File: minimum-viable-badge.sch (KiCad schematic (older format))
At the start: 33 parts, among them J101 EDGE_CONNECTOR, P101 USB, P102 BATTERY, P103 POT_LONG, P104 BUTTON_A, P105 BUTTON_B, P106 POT_SHORT, P107 MECH, P108 MECH, P109 MECH, Q101 S8050, Q102 S8050, SW101 PRGM, SW102 RESET, U101 ESP32-WROOM, U102 CP2102

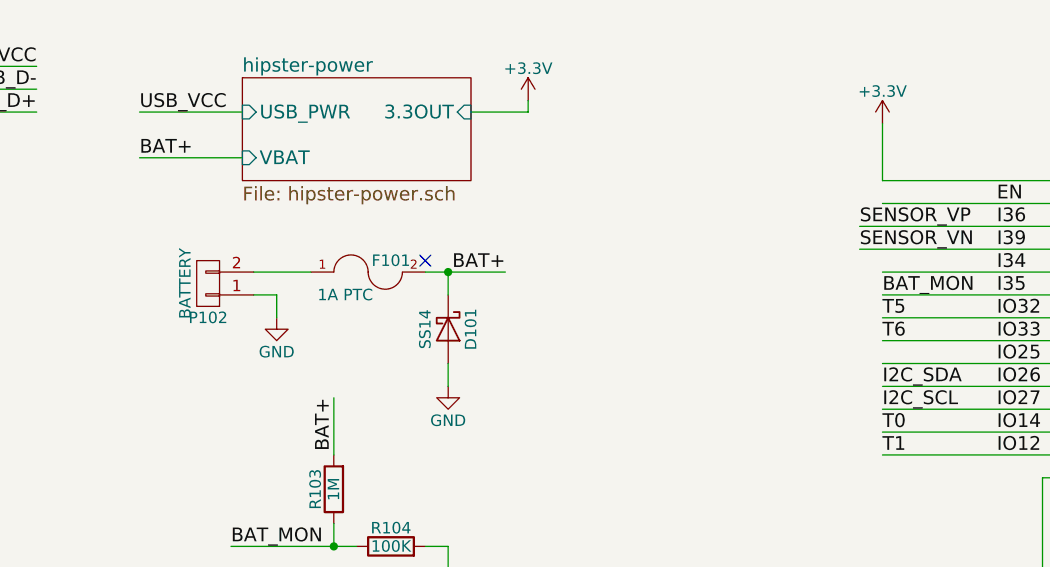
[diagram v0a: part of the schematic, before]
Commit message: Swap battery connector to JST PH 2.0
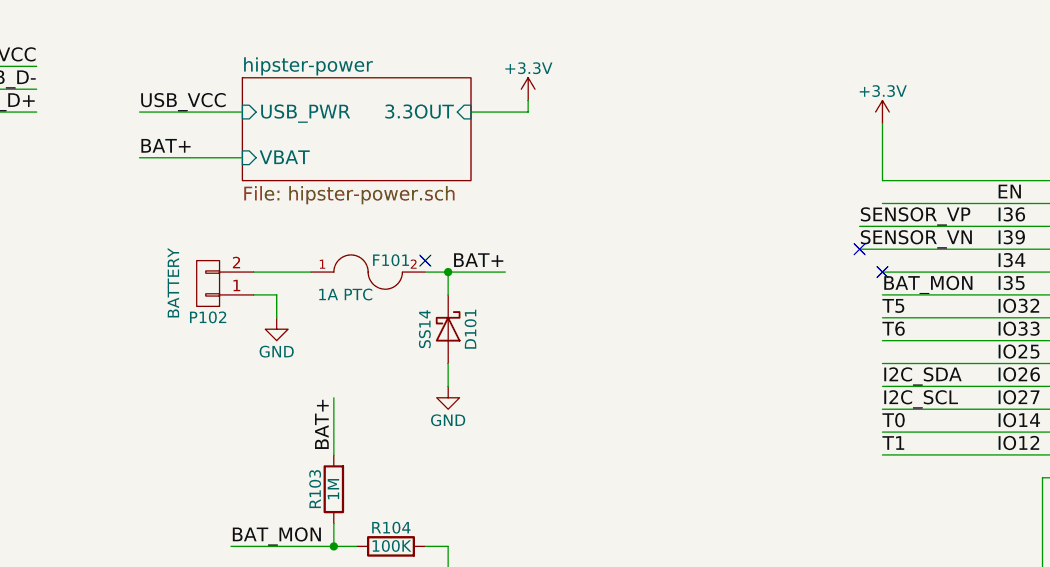
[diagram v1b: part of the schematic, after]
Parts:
- P102: footprint Pin_Headers:Pin_Header_Angled_1x02_Pitch2.54mm -> Connectors_JST:JST_PH_S2B-PH-K_02x2.00mm_Angled
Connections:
- no-connect marks 19 -> 21
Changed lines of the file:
@@
 P 2650 2100
 F 0 "P102" H 2650 2250 50  0000 C CNN
-F 1 "BATTERY" V 2750 2100 50  0000 C CNN
-F 2 "Pin_Headers:Pin_Header_Angled_1x02_Pitch2.54mm" H 2650 2100 50  0001 C CNN
+F 1 "BATTERY" V 2800 2100 50  0000 C CNN
+F 2 "Connectors_JST:JST_PH_S2B-PH-K_02x2.00mm_Angled" H 2650 2100 50  0001 C CNN
 F 3 "" H 2650 2100 50  0000 C CNN
 	1    2650 2100
@@
 Text Label 8550 1900 2    60   ~ 0
 IO21
+NoConn ~ 5500 1950
+NoConn ~ 5600 2050
 $EndSCHEMATC

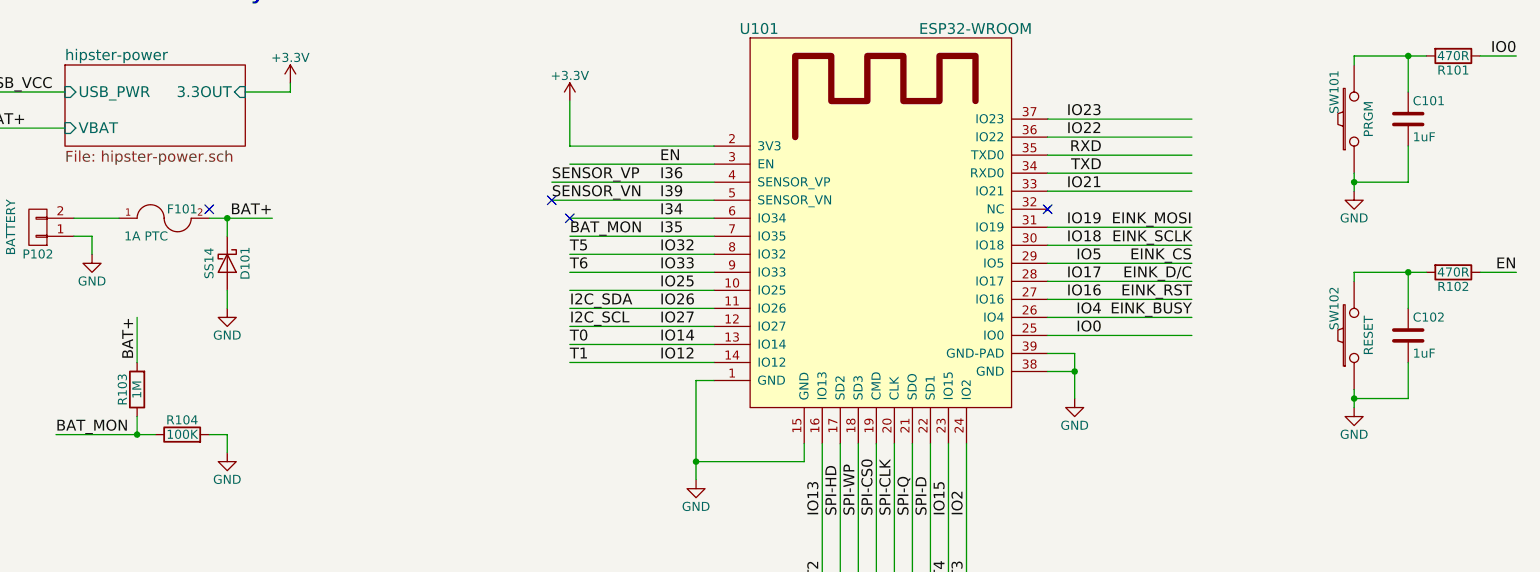
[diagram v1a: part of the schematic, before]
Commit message: Add SZLCSC part links
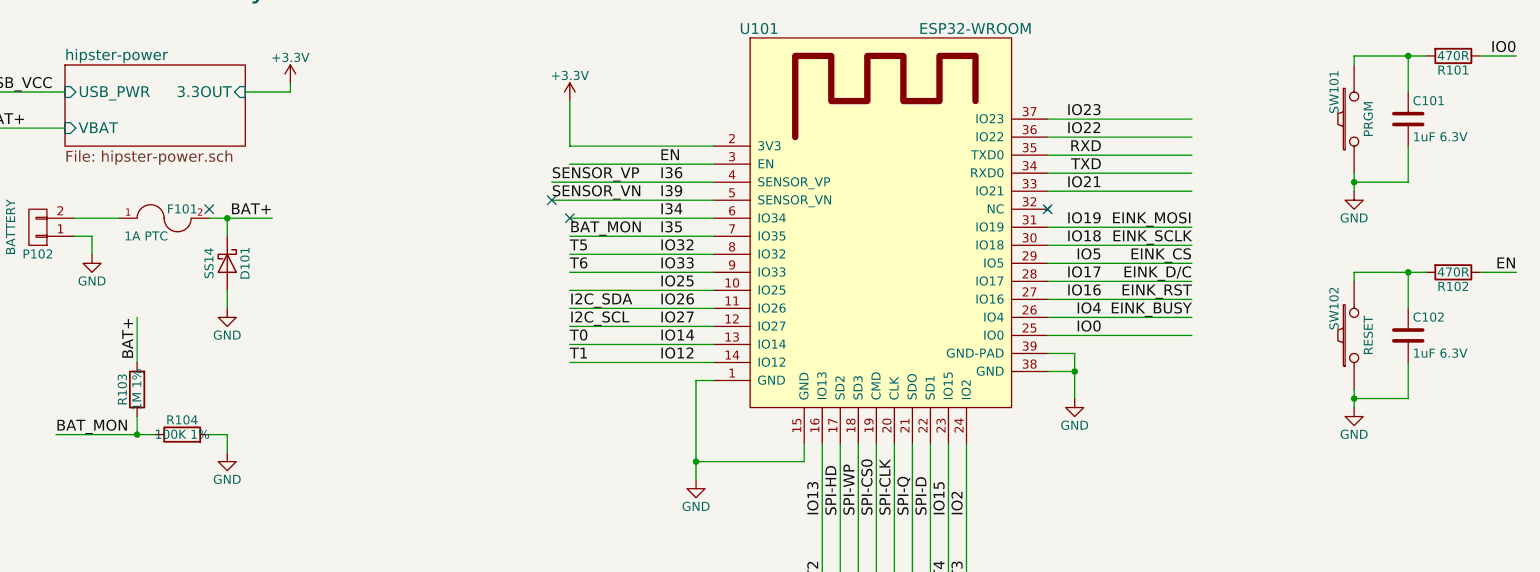
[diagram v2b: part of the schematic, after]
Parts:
- C101, C102: value 1uF -> 1uF 6.3V; LCSC (none) -> http://www.szlcsc.com/product/details_94382.html
- C103: LCSC (none) -> http://www.szlcsc.com/product/details_94382.html
- C104, C106: LCSC (none) -> http://www.szlcsc.com/product/details_42881.html
- C105, C107: LCSC (none) -> http://www.szlcsc.com/product/details_2040.html
- D101: LCSC (none) -> http://www.szlcsc.com/product/details_85512.html
- F101: LCSC (none) -> http://www.szlcsc.com/product/details_72573.html
- Q101, Q102: LCSC (none) -> http://www.szlcsc.com/product/details_106648.html
- R101, R102, R105: LCSC (none) -> http://www.szlcsc.com/product/details_25984.html
- R103: value 1M -> 1M 1%; LCSC (none) -> http://www.szlcsc.com/product/details_106793.html
- R104: value 100K -> 100K 1%; LCSC (none) -> http://www.szlcsc.com/product/details_26546.html
- R106, R107, R108: LCSC (none) -> http://www.szlcsc.com/product/details_101951.html
- SW101, SW102: LCSC (none) -> http://www.szlcsc.com/product/details_119400.html
- U101: LCSC (none) -> http://www.szlcsc.com/product/details_96410.html
- U102: LCSC (none) -> http://www.szlcsc.com/product/details_7033.html
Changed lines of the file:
@@
 F 2 "ESP32-footprints-Lib:ESP32-WROOM" H 7700 3600 60  0001 C CNN
 F 3 "" H 6900 2700 60  0001 C CNN
+F 4 "http://www.szlcsc.com/product/details_96410.html" H 7350 2250 60  0001 C CNN "LCSC"
 	1    7350 2250
 	1    0    0    -1
@@
 F 6 "RC0603FR-07470RL" V 10600 1150 60  0001 C CNN "Manufacturer PN"
 F 7 "0.10" V 10600 1150 60  0001 C CNN "Unit Cost"
+F 8 "http://www.szlcsc.com/product/details_25984.html" H 7350 2250 60  0001 C CNN "LCSC"
 	1    10500 1150
 	0    1    1    0
@@
 P 10250 1500
 F 0 "C101" H 10275 1600 50  0000 L CNN
-F 1 "1uF" H 10275 1400 50  0000 L CNN
+F 1 "1uF 6.3V" H 10275 1400 50  0000 L CNN
 F 2 "Capacitors_SMD:C_0603_HandSoldering" H 10288 1350 50  0001 C CNN
 F 3 "" H 10250 1500 50  0000 C CNN
+F 4 "http://www.szlcsc.com/product/details_94382.html" H 7350 2250 60  0001 C CNN "LCSC"
 	1    10250 1500
 	1    0    0    -1
@@
 F 2 "libs:K2-1107st" H 9950 1500 50  0001 C CNN
 F 3 "" H 9950 1500 50  0000 C CNN
+F 4 "http://www.szlcsc.com/product/details_119400.html" H 7350 2250 60  0001 C CNN "LCSC"
 	1    9950 1500
 	0    -1   -1   0
@@
 F 6 "RC0603FR-07470RL" V 10600 1150 60  0001 C CNN "Manufacturer PN"
 F 7 "0.10" V 10600 1150 60  0001 C CNN "Unit Cost"
+F 8 "http://www.szlcsc.com/product/details_25984.html" H 7350 2250 60  0001 C CNN "LCSC"
 	1    10500 2350
 	0    1    1    0
@@
 P 10250 2700
 F 0 "C102" H 10275 2800 50  0000 L CNN
-F 1 "1uF" H 10275 2600 50  0000 L CNN
+F 1 "1uF 6.3V" H 10275 2600 50  0000 L CNN
 F 2 "Capacitors_SMD:C_0603_HandSoldering" H 10288 2550 50  0001 C CNN
 F 3 "" H 10250 2700 50  0000 C CNN
+F 4 "http://www.szlcsc.com/product/details_94382.html" H 7350 2250 60  0001 C CNN "LCSC"
 	1    10250 2700
 	1    0    0    -1
@@
 F 2 "libs:K2-1107st" H 9950 2700 50  0001 C CNN
 F 3 "" H 9950 2700 50  0000 C CNN
+F 4 "http://www.szlcsc.com/product/details_119400.html" H 7350 2250 60  0001 C CNN "LCSC"
 	1    9950 2700
 	0    -1   -1   0
@@
 F 6 "RC0603FR-0712KL" V -5300 6300 60  0001 C CNN "Manufacturer PN"
 F 7 "0.10" V -5300 6300 60  0001 C CNN "Unit Cost"
+F 8 "http://www.szlcsc.com/product/details_101951.html" H 7350 2250 60  0001 C CNN "LCSC"
 	1    4100 4900
 	-1   0    0    1
@@
 F 6 "CP2102-GMR" H 1800 6050 60  0001 C CNN "Manufacturer PN"
 F 7 "2.88" H 1800 6050 60  0001 C CNN "Unit Cost"
+F 8 "http://www.szlcsc.com/product/details_7033.html" H 7350 2250 60  0001 C CNN "LCSC"
 	1    2150 5850
 	1    0    0    -1
@@
 F 6 "CC0603KRX7R7BB104" H 300 6400 60  0001 C CNN "Manufacturer PN"
 F 7 "0.10" H 300 6400 60  0001 C CNN "Unit Cost"
+F 8 "http://www.szlcsc.com/product/details_2040.html" H 7350 2250 60  0001 C CNN "LCSC"
 	1    1850 6950
 	1    0    0    -1
@@
 F 6 "CL21A106KOCLRNC" H -50 6400 60  0001 C CNN "Manufacturer PN"
 F 7 "0.18" H -50 6400 60  0001 C CNN "Unit Cost"
+F 8 "http://www.szlcsc.com/product/details_42881.html" H 7350 2250 60  0001 C CNN "LCSC"
 	1    1550 6950
 	1    0    0    -1
@@
 F 6 "CC0603KRX7R7BB104" H 300 6400 60  0001 C CNN "Manufacturer PN"
 F 7 "0.10" H 300 6400 60  0001 C CNN "Unit Cost"
+F 8 "http://www.szlcsc.com/product/details_2040.html" H 7350 2250 60  0001 C CNN "LCSC"
 	1    1150 6500
 	1    0    0    -1
@@
 F 6 "CL21A106KOCLRNC" H -50 6400 60  0001 C CNN "Manufacturer PN"
 F 7 "0.18" H -50 6400 60  0001 C CNN "Unit Cost"
+F 8 "http://www.szlcsc.com/product/details_42881.html" H 7350 2250 60  0001 C CNN "LCSC"
 	1    850  6500
 	1    0    0    -1
@@
 F 6 "RC0603FR-07470RL" V 8800 650 60  0001 C CNN "Manufacturer PN"
 F 7 "0.10" V 8800 650 60  0001 C CNN "Unit Cost"
+F 8 "http://www.szlcsc.com/product/details_25984.html" H 7350 2250 60  0001 C CNN "LCSC"
 	1    2300 4550
 	0    1    1    0
@@
 F 6 "RC0603FR-0712KL" V 3550 5250 60  0001 C CNN "Manufacturer PN"
 F 7 "0.10" V 3550 5250 60  0001 C CNN "Unit Cost"
+F 8 "http://www.szlcsc.com/product/details_101951.html" H 7350 2250 60  0001 C CNN "LCSC"
 	1    3850 6850
 	0    1    1    0
@@
 F 6 "RC0603FR-0712KL" V 3550 5250 60  0001 C CNN "Manufacturer PN"
 F 7 "0.10" V 3550 5250 60  0001 C CNN "Unit Cost"
+F 8 "http://www.szlcsc.com/product/details_101951.html" H 7350 2250 60  0001 C CNN "LCSC"
 	1    3850 6150
 	0    1    1    0
@@
 P 3200 3000
 F 0 "R103" V 3280 3000 50  0000 C CNN
-F 1 "1M" V 3200 3000 50  0000 C CNN
+F 1 "1M 1%" V 3200 3000 50  0000 C CNN
 F 2 "Resistors_SMD:R_0603_HandSoldering" V 3130 3000 50  0001 C CNN
 F 3 "" H 3200 3000 50  0000 C CNN
@@
 F 6 "RC0603FR-071ML" V 3000 2100 60  0001 C CNN "Manufacturer PN"
 F 7 "0.10" V 3000 2100 60  0001 C CNN "Unit Cost"
+F 8 "http://www.szlcsc.com/product/details_106793.html" H 7350 2250 60  0001 C CNN "LCSC"
 	1    3200 3000
 	-1   0    0    1
@@
 P 3450 3250
 F 0 "R104" V 3530 3250 50  0000 C CNN
-F 1 "100K" V 3450 3250 50  0000 C CNN
+F 1 "100K 1%" V 3450 3250 50  0000 C CNN
 F 2 "Resistors_SMD:R_0603_HandSoldering" V 3380 3250 50  0001 C CNN
 F 3 "" H 3450 3250 50  0000 C CNN
@@
 F 6 "RC0603JR-07100KL" V 3250 2350 60  0001 C CNN "Manufacturer PN"
 F 7 "0.10" V 3250 2350 60  0001 C CNN "Unit Cost"
+F 8 "http://www.szlcsc.com/product/details_26546.html" H 7350 2250 60  0001 C CNN "LCSC"
 	1    3450 3250
 	0    -1   -1   0
@@
 F 6 "0ZCH0050FF2G" H 3450 300 60  0001 C CNN "Manufacturer PN"
 F 7 "0.12" H 3450 300 60  0001 C CNN "Unit Cost"
+F 8 "http://www.szlcsc.com/product/details_72573.html" H 7350 2250 60  0001 C CNN "LCSC"
 	1    3350 2050
 	1    0    0    -1
@@
 F 6 "SS14" H 3800 600 60  0001 C CNN "Manufacturer PN"
 F 7 "0.39" H 3800 600 60  0001 C CNN "Unit Cost"
+F 8 "http://www.szlcsc.com/product/details_85512.html" H 7350 2250 60  0001 C CNN "LCSC"
 	1    3700 2300
 	0    1    1    0
@@
 F 6 "MMSS8050-H-TP" H 4400 6150 60  0001 C CNN "Manufacture PN"
 F 7 "0.20" H 4400 6150 60  0001 C CNN "Cost"
+F 8 "http://www.szlcsc.com/product/details_106648.html" H 7350 2250 60  0001 C CNN "LCSC"
 	1    4400 6150
 	1    0    0    -1
@@
 F 6 "MMSS8050-H-TP" H 4400 6150 60  0001 C CNN "Manufacture PN"
 F 7 "0.20" H 4400 6150 60  0001 C CNN "Cost"
+F 8 "http://www.szlcsc.com/product/details_106648.html" H 7350 2250 60  0001 C CNN "LCSC"
 	1    4400 6850
 	1    0    0    1
@@
 F 2 "Capacitors_SMD:C_0603_HandSoldering" H 4138 5250 50  0001 C CNN
 F 3 "" H 4100 5400 50  0000 C CNN
+F 4 "http://www.szlcsc.com/product/details_94382.html" H 7350 2250 60  0001 C CNN "LCSC"
 	1    4100 5400
 	1    0    0    -1

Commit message: Added edge connector and button silkscreen
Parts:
- J101: footprint Pin_Headers:Pin_Header_Angled_1x10_Pitch2.54mm -> libs:Edge_Connector_1x10_Pitch2.54mm
- P104, P105: footprint Mounting_Holes:MountingHole_3.2mm_M3_Pad -> libs:buttons
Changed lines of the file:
@@
 F 0 "P104" H 10500 5250 50  0000 C CNN
 F 1 "BUTTON_A" H 10350 5050 50  0000 C CNN
-F 2 "Mounting_Holes:MountingHole_3.2mm_M3_Pad" H 10500 5150 50  0001 C CNN
+F 2 "libs:buttons" H 10500 5150 50  0001 C CNN
 F 3 "" H 10500 5150 50  0000 C CNN
 	1    10500 5150
@@
 F 0 "P105" H 10500 5550 50  0000 C CNN
 F 1 "BUTTON_B" H 10350 5350 50  0000 C CNN
-F 2 "Mounting_Holes:MountingHole_3.2mm_M3_Pad" H 10500 5450 50  0001 C CNN
+F 2 "libs:buttons" H 10500 5450 50  0001 C CNN
 F 3 "" H 10500 5450 50  0000 C CNN
 	1    10500 5450
@@
 F 0 "J101" H 7650 6200 50  0000 C CNN
 F 1 "EDGE_CONNECTOR" V 7750 5650 50  0000 C CNN
-F 2 "Pin_Headers:Pin_Header_Angled_1x10_Pitch2.54mm" H 7650 5650 50  0001 C CNN
+F 2 "libs:Edge_Connector_1x10_Pitch2.54mm" H 7650 5650 50  0001 C CNN
 F 3 "" H 7650 5650 50  0001 C CNN
 	1    7650 5650

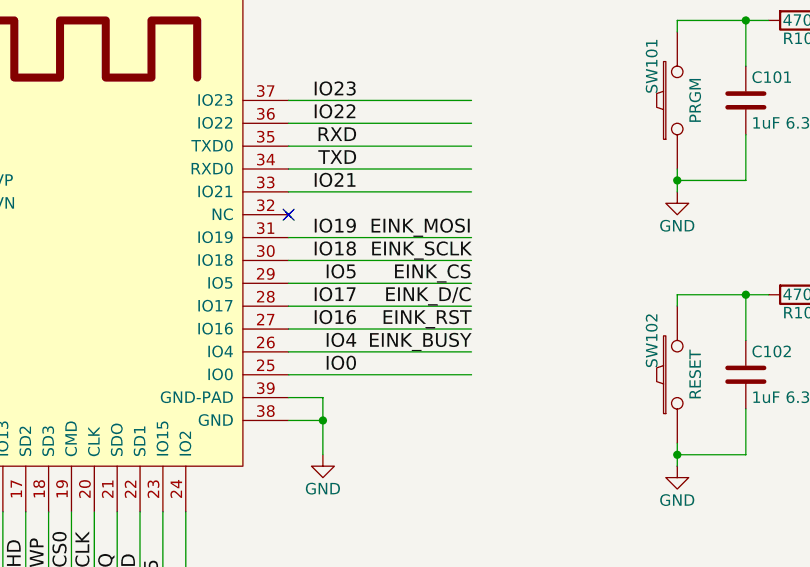
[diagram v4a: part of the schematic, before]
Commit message: Correct e-ink connector direction, reposition & reroute board
Closes #20
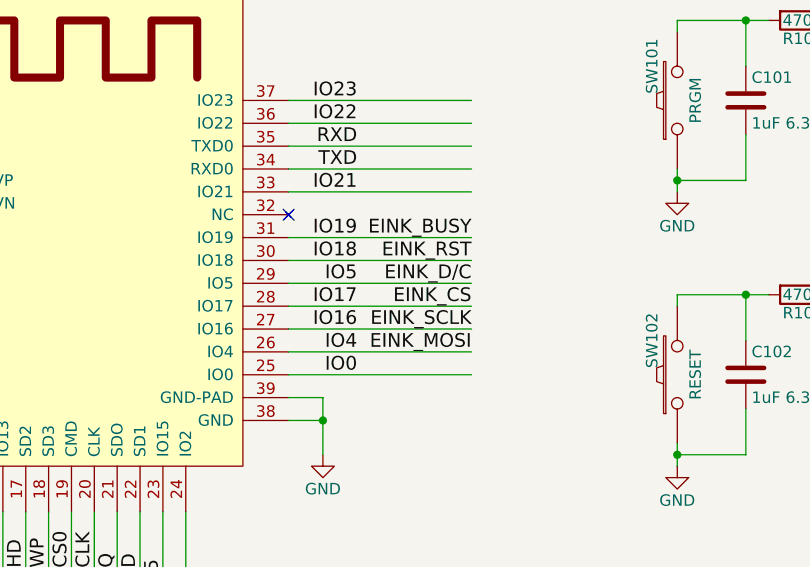
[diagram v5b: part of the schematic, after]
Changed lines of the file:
@@
 	1    0    0    -1
 $EndComp
+Text Label 9050 2100 2    60   ~ 0
+EINK_BUSY
+Text Label 9050 2200 2    60   ~ 0
+EINK_RST
+Text Label 9050 2300 2    60   ~ 0
+EINK_D/C
+Text Label 9050 2400 2    60   ~ 0
+EINK_CS
+Text Label 9050 2500 2    60   ~ 0
+EINK_SCLK
 Text Label 9050 2600 2    60   ~ 0
-EINK_BUSY
-Text Label 9050 2500 2    60   ~ 0
-EINK_RST
-Text Label 9050 2400 2    60   ~ 0
-EINK_D/C
-Text Label 9050 2300 2    60   ~ 0
-EINK_CS
-Text Label 9050 2200 2    60   ~ 0
-EINK_SCLK
-Text Label 9050 2100 2    60   ~ 0
 EINK_MOSI
 Wire Wire Line
@@
 	8250 2700 9050 2700
 Wire Wire Line
-	8250 2600 9050 2600
+	8250 2100 9050 2100
+Wire Wire Line
+	8250 2200 9050 2200
+Wire Wire Line
+	8250 2300 9050 2300
+Wire Wire Line
+	8250 2400 9050 2400
 Wire Wire Line
 	8250 2500 9050 2500
 Wire Wire Line
-	8250 2400 9050 2400
-Wire Wire Line
-	8250 2300 9050 2300
-Wire Wire Line
-	8250 2200 9050 2200
-Wire Wire Line
-	8250 2100 9050 2100
+	8250 2600 9050 2600
 Wire Wire Line
 	8250 1900 9050 1900
